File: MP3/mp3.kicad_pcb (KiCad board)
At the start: 2 copper layers, 18 x 51.5 mm, 38 parts, among them J1 USB4105-GF-A, J2 LEFT, J3 DEBUG, J4 RIGHT, U1 W25Q128JV, U2 RP2040, U3 MCP1702T-3302E_CB, Y1 12MHz

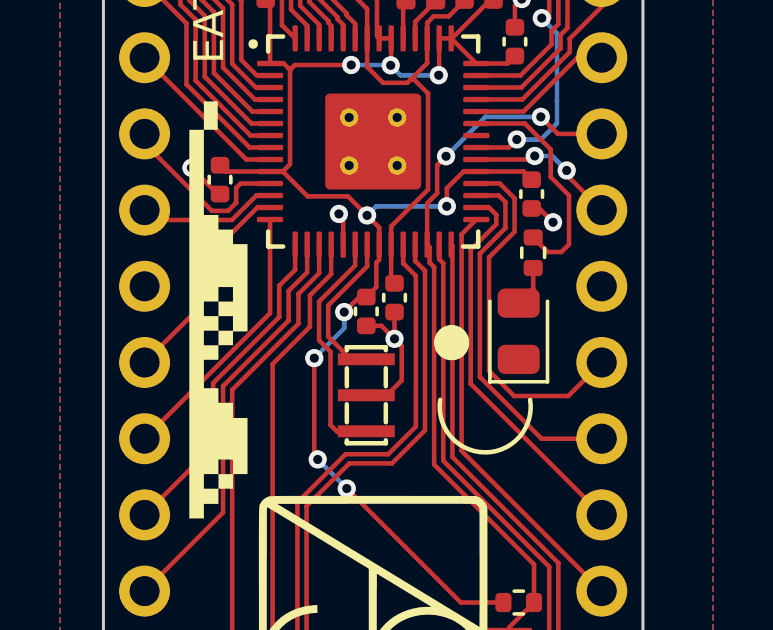
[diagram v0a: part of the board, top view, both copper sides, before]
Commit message: move C10 down a little for looks
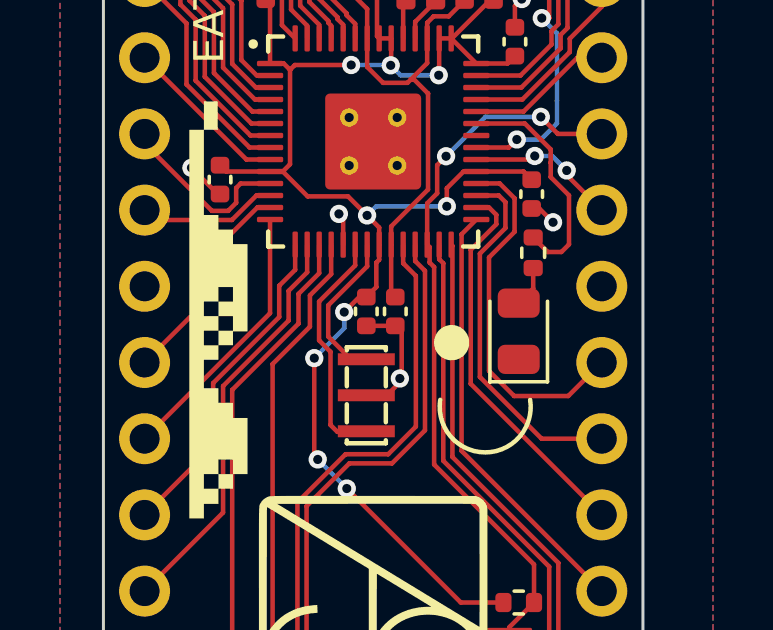
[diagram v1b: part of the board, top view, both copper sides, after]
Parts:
- moved C10 0.46 mm to (116.6, 104.1)
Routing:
- net GND: track 31.1 -> 30.5 mm
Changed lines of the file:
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@@
   )
   (footprint "Capacitor_SMD:C_0402_1005Metric" (layer "F.Cu")
-    (at 116.5352 103.632 -90)
+    (at 116.5606 104.0892 -90)
     (descr "Capacitor SMD 0402 (1005 Metric), square (rectangular) end terminal, IPC_7351 nominal, (Body size source: IPC-SM-782 page 76, https://www.pcb-3d.com/wordpress/wp-content/uploads/ipc-sm-782a_amendment_1_and_2.pdf), generated with kicad-footprint-generator")
     (tags "capacitor")
@@
   (segment (start 111.504 78.001) (end 111.504 79.9889) (width 0.635) (layer "F.Cu") (net 1))
   (segment (start 119.024 78.576) (end 119.569 78.576) (width 0.635) (layer "F.Cu") (net 1))
-  (segment (start 116.1008 104.5692) (end 116.5352 105.0036) (width 0.1524) (layer "F.Cu") (net 1))
   (segment (start 110.7186 100.175) (end 110.640956 100.175) (width 0.1524) (layer "F.Cu") (net 1))
+  (segment (start 116.774 106.2639) (end 116.7135 106.3244) (width 0.1524) (layer "F.Cu") (net 1))
   (segment (start 114.2492 81.1784) (end 114.9096 81.8388) (width 0.1524) (layer "F.Cu") (net 1))
   (segment (start 114.824 100.981) (end 114.681 100.838) (width 0.1524) (layer "F.Cu") (net 1))
   (segment (start 114.824 101.8625) (end 114.824 100.981) (width 0.1524) (layer "F.Cu") (net 1))
   (segment (start 121.1072 100.6576) (end 121.3591 100.6576) (width 0.1524) (layer "F.Cu") (net 1))
-  (segment (start 116.5352 105.0036) (end 116.774 105.2424) (width 0.1524) (layer "F.Cu") (net 1))
-  (segment (start 116.2812 106.8832) (end 115.5954 106.8832) (width 0.1524) (layer "F.Cu") (net 1))
+  (segment (start 116.774 104.7826) (end 116.774 106.2639) (width 0.1524) (layer "F.Cu") (net 1))
   (segment (start 114.9096 88.0364) (end 115.3668 88.4936) (width 0.1524) (layer "F.Cu") (net 1))
   (segment (start 119.031379 84.419079) (end 119.842282 84.419079) (width 0.1524) (layer "F.Cu") (net 1))
@@
   (segment (start 120.5484 93.9038) (end 120.777 93.6752) (width 0.1524) (layer "F.Cu") (net 1))
   (segment (start 118.9634 84.3511) (end 119.031379 84.419079) (width 0.1524) (layer "F.Cu") (net 1))
-  (segment (start 115.5954 104.5692) (end 116.1008 104.5692) (width 0.1524) (layer "F.Cu") (net 1))
-  (segment (start 116.5352 104.112) (end 116.5352 105.0036) (width 0.1524) (layer "F.Cu") (net 1))
   (segment (start 111.504 79.9889) (end 111.0511 80.4418) (width 0.635) (layer "F.Cu") (net 1))
   (segment (start 110.640956 100.175) (end 109.766678 99.300722) (width 0.1524) (layer "F.Cu") (net 1))
   (segment (start 115.7504 85.3694) (end 115.603058 85.3694) (width 0.1524) (layer "F.Cu") (net 1))
+  (segment (start 116.774 106.3849) (end 116.774 106.3904) (width 0.1524) (layer "F.Cu") (net 1))
   (segment (start 120.904 88.773) (end 121.158 89.027) (width 0.1524) (layer "F.Cu") (net 1))
   (segment (start 111.565491 92.738) (end 112.2426 92.738) (width 0.1524) (layer "F.Cu") (net 1))
@@
   (segment (start 121.3591 100.6576) (end 121.8189 101.1174) (width 0.1524) (layer "F.Cu") (net 1))
   (segment (start 119.024 79.8958) (end 118.6558 80.264) (width 0.1524) (layer "F.Cu") (net 1))
+  (segment (start 116.7135 106.3244) (end 116.774 106.3849) (width 0.1524) (layer "F.Cu") (net 1))
+  (segment (start 115.5954 104.5692) (end 116.5606 104.5692) (width 0.1524) (layer "F.Cu") (net 1))
   (segment (start 114.9604 85.3694) (end 115.7504 85.3694) (width 0.1524) (layer "F.Cu") (net 1))
   (segment (start 116.1892 92.4332) (end 116.6622 91.9602) (width 0.1524) (layer "F.Cu") (net 1))
@@
   (segment (start 119.024 78.576) (end 119.024 79.8958) (width 0.1524) (layer "F.Cu") (net 1))
   (segment (start 115.603058 85.3694) (end 114.9096 86.062858) (width 0.1524) (layer "F.Cu") (net 1))
+  (segment (start 116.5606 104.5692) (end 116.774 104.7826) (width 0.1524) (layer "F.Cu") (net 1))
   (segment (start 112.079 78.576) (end 111.504 78.001) (width 0.254) (layer "F.Cu") (net 1))
-  (segment (start 116.774 105.2424) (end 116.774 106.3904) (width 0.1524) (layer "F.Cu") (net 1))
   (segment (start 114.2492 80.9264) (end 114.2492 81.1784) (width 0.1524) (layer "F.Cu") (net 1))
   (segment (start 116.774 106.3904) (end 116.2812 106.8832) (width 0.1524) (layer "F.Cu") (net 1))
+  (segment (start 116.2812 106.8832) (end 115.5954 106.8832) (width 0.1524) (layer "F.Cu") (net 1))
   (segment (start 115.951 92.4332) (end 116.1892 92.4332) (width 0.1524) (layer "F.Cu") (net 1))
   (segment (start 117.9934 80.9264) (end 118.6558 80.264) (width 0.1524) (layer "F.Cu") (net 1))
@@
   (via (at 120.5484 119.507) (size 0.6096) (drill 0.3048) (layers "F.Cu" "B.Cu") (free) (net 1))
   (via (at 121.8189 101.1174) (size 0.6096) (drill 0.3048) (layers "F.Cu" "B.Cu") (net 1))
-  (via (at 116.5352 105.0036) (size 0.6096) (drill 0.3048) (layers "F.Cu" "B.Cu") (net 1))
+  (via (at 116.7135 106.3244) (size 0.6096) (drill 0.3048) (layers "F.Cu" "B.Cu") (net 1))
   (segment (start 118.424 94.9875) (end 119.2615 95.825) (width 0.1524) (layer "F.Cu") (net 2))
   (segment (start 119.2615 99.425) (end 118.837071 99.425) (width 0.1524) (layer "F.Cu") (net 2))
@@
   (segment (start 117.652037 96.824037) (end 117.1829 96.3549) (width 0.1524) (layer "F.Cu") (net 3))
   (segment (start 117.0813 96.3549) (end 117.624 95.8122) (width 0.1524) (layer "F.Cu") (net 3))
+  (segment (start 116.424 101.8625) (end 116.424 103.4726) (width 0.1524) (layer "F.Cu") (net 3))
   (segment (start 117.1829 96.3549) (end 117.0813 96.3549) (width 0.1524) (layer "F.Cu") (net 3))
   (segment (start 115.624 94.9875) (end 115.624 95.939) (width 0.1524) (layer "F.Cu") (net 3))
-  (segment (start 116.424 101.8625) (end 116.424 103.0408) (width 0.1524) (layer "F.Cu") (net 3))
+  (segment (start 116.424 103.4726) (end 116.5606 103.6092) (width 0.1524) (layer "F.Cu") (net 3))
   (segment (start 116.1542 96.4692) (end 116.967 96.4692) (width 0.1524) (layer "F.Cu") (net 3))
   (segment (start 117.624 94.467252) (end 117.839252 94.252) (width 0.1524) (layer "F.Cu") (net 3))
@@
   (segment (start 117.624 95.8122) (end 117.624 94.9875) (width 0.1524) (layer "F.Cu") (net 3))
   (segment (start 118.3434 94.252) (end 118.872 93.7234) (width 0.1524) (layer "F.Cu") (net 3))
-  (segment (start 116.424 103.0408) (end 116.5352 103.152) (width 0.1524) (layer "F.Cu") (net 3))
   (segment (start 116.967 96.4692) (end 117.0813 96.3549) (width 0.1524) (layer "F.Cu") (net 3))
   (segment (start 116.424 101.254563) (end 117.6526 100.025963) (width 0.1524) (layer "F.Cu") (net 3))
